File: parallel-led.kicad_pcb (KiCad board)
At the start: 2 copper layers, 97 x 98 mm, 11 parts

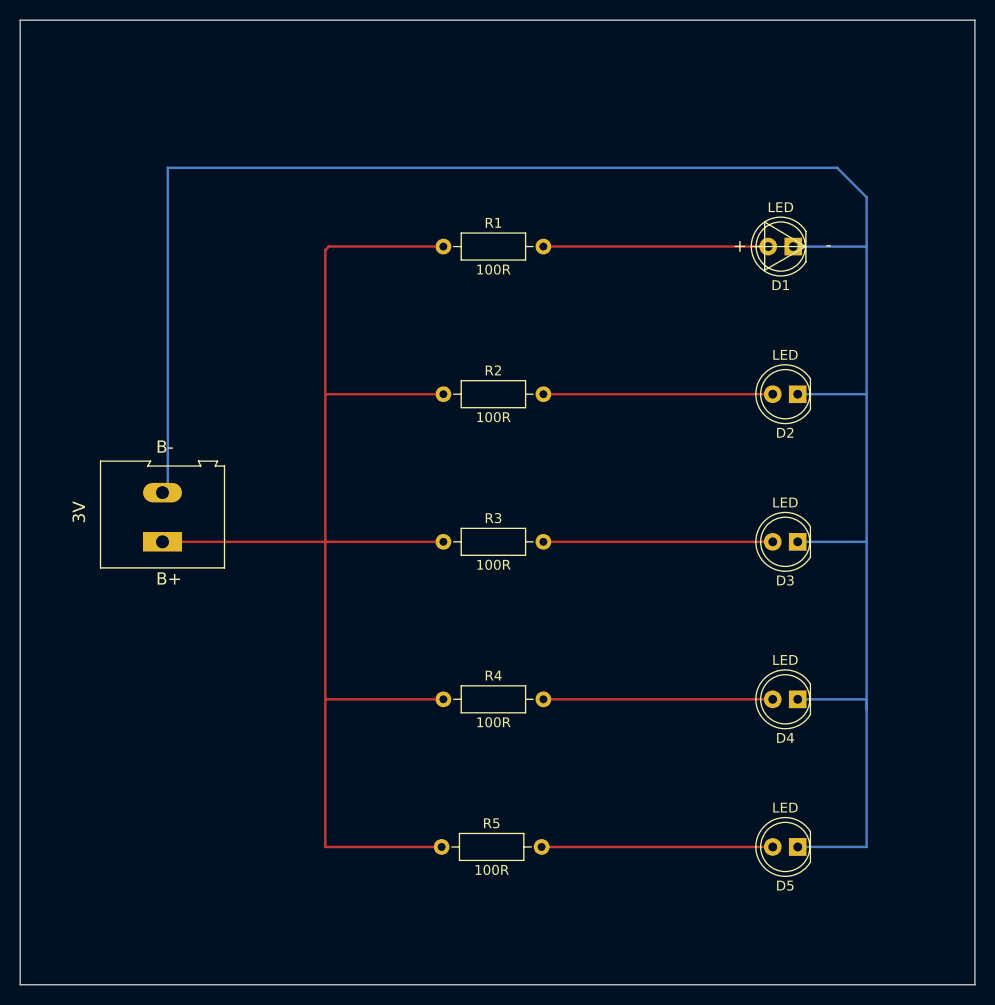
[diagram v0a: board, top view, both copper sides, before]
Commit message: replace led with custom footprint
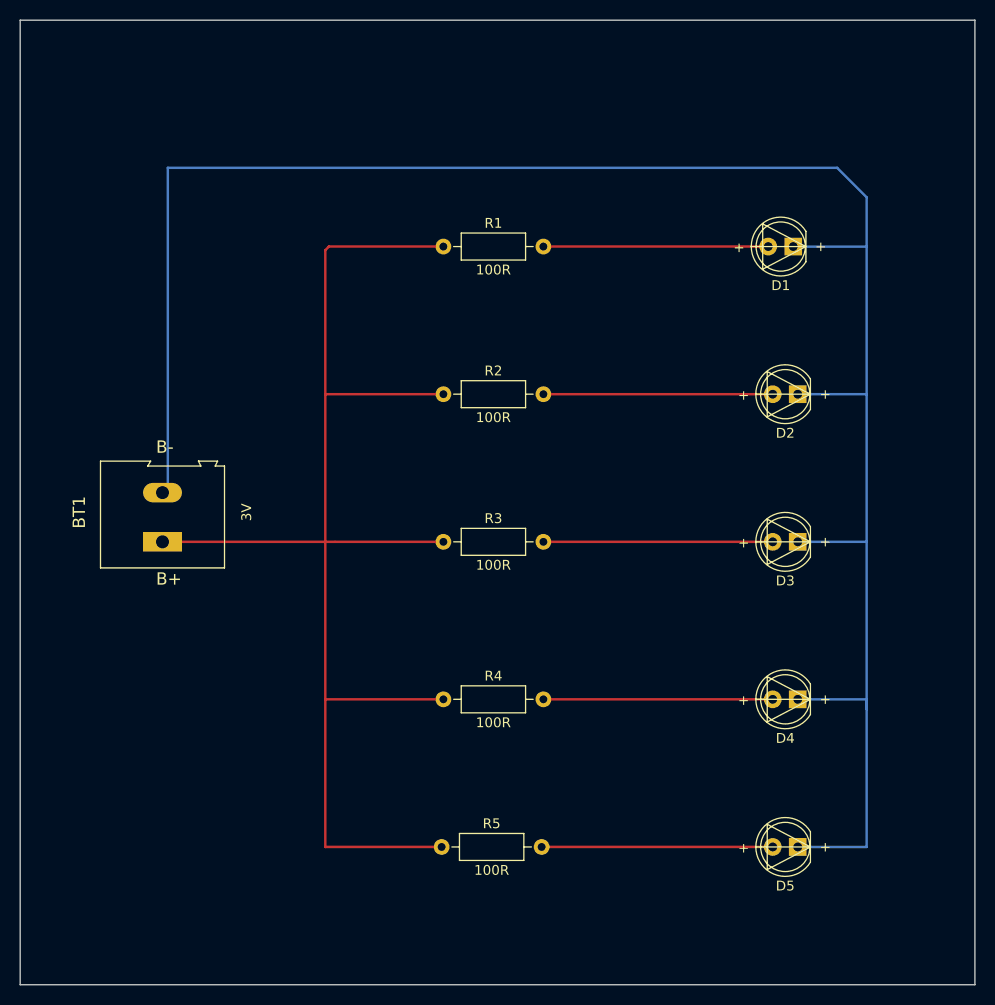
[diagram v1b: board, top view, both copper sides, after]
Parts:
- D1, D2, D3, D4, D5: footprint LED_THT:LED_D5.0mm -> BeginnerModules:BeginnerLED_D5.0mm
- renumbered 3V to BT1
